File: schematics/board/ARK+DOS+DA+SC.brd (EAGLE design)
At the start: 82 x 92 mm, 210 parts, among them IC2 STM32F103C8T

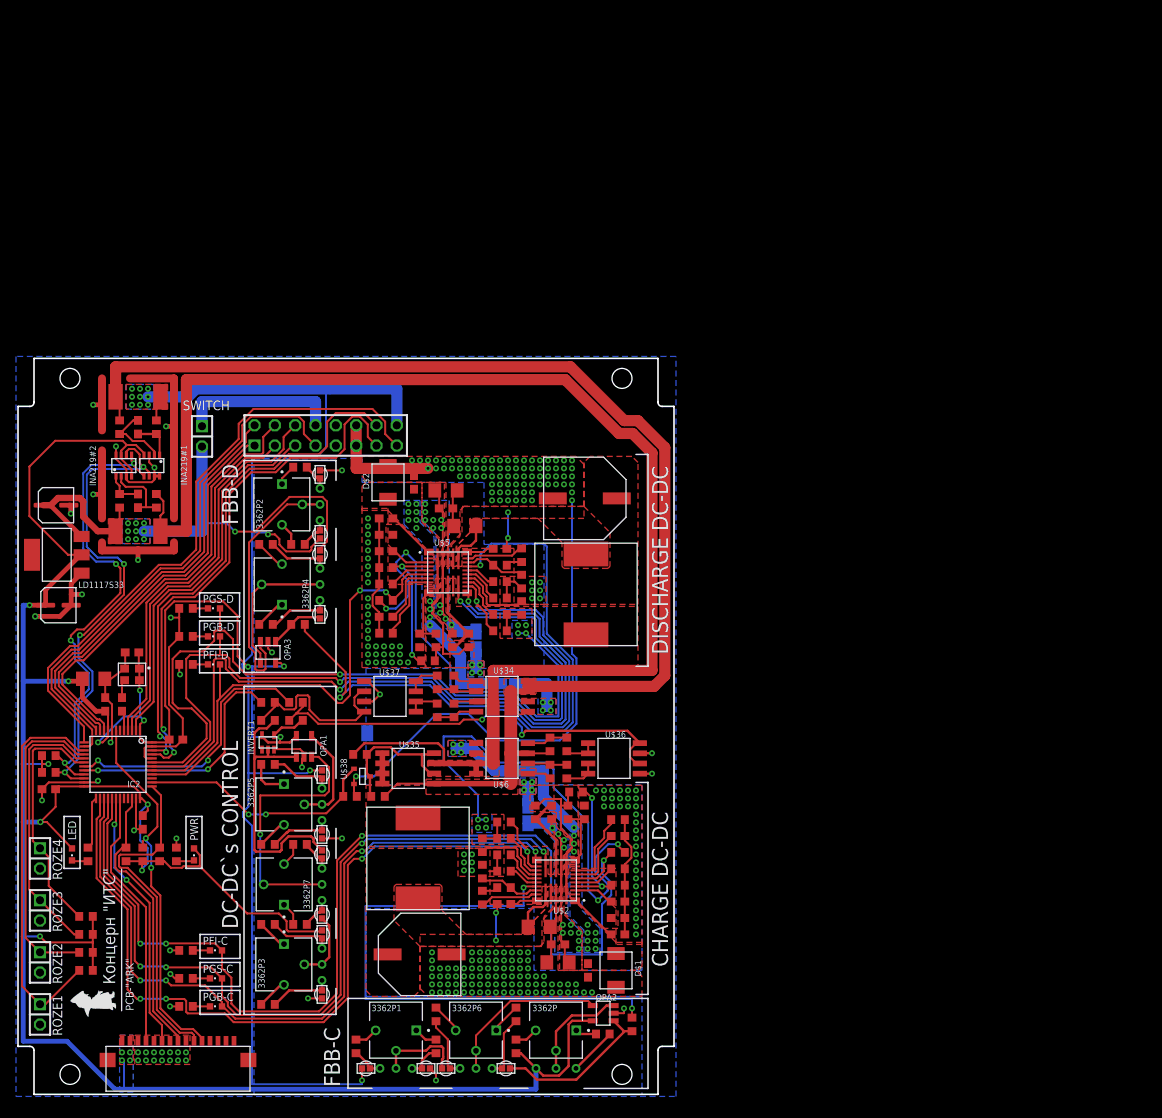
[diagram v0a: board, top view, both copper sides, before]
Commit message: Плата АРК и платы регулярок отправлены в производство
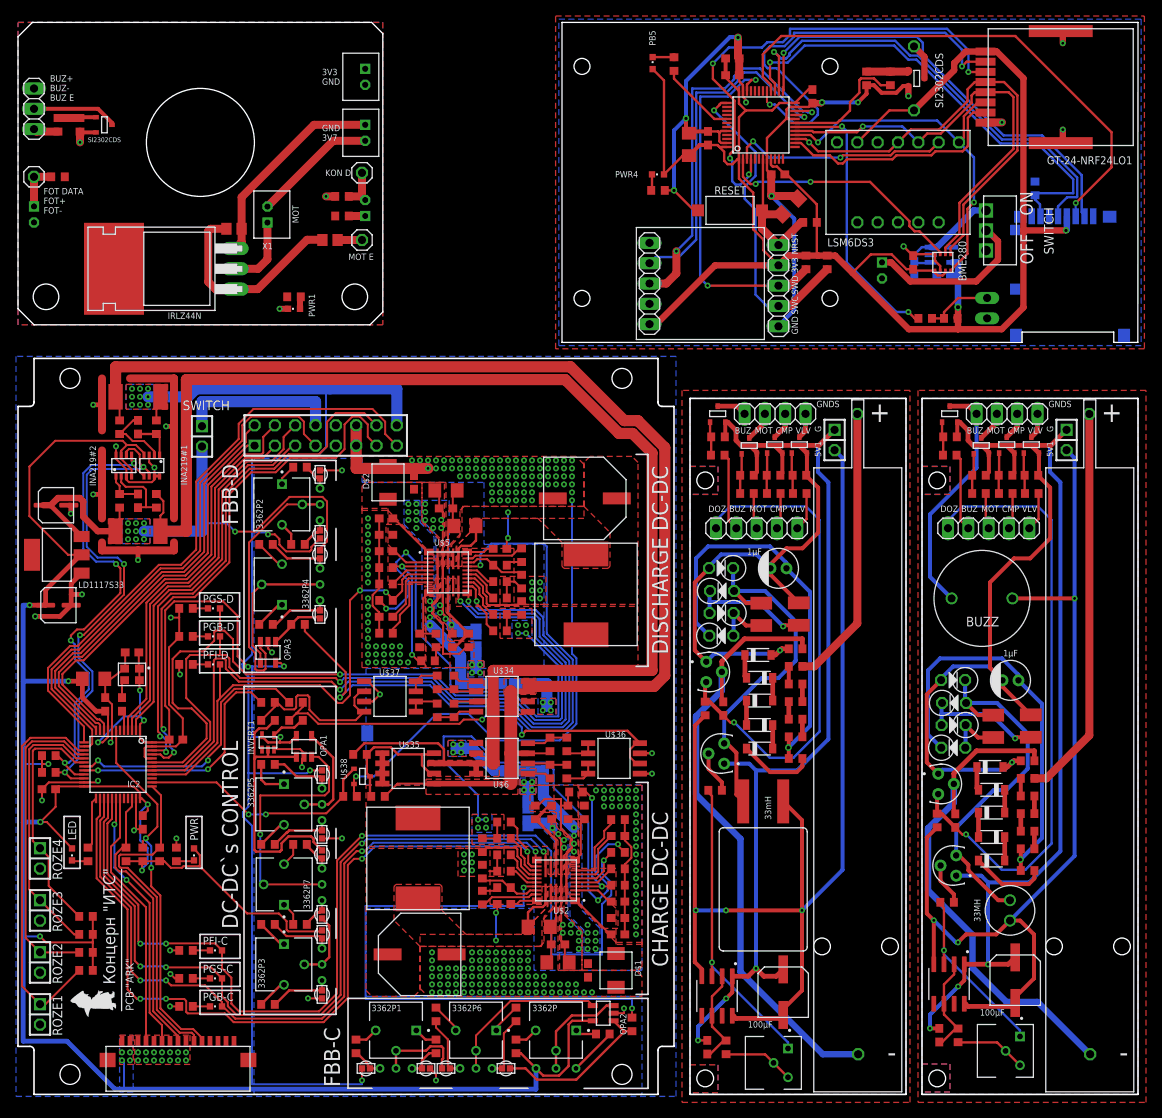
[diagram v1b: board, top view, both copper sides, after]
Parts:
- added BME280: BME280CHIP, CanCubeSat:BME280CHIP
- added BUZZ: BUZZER, CanCubeSat:BUZZER
- added BUZZER: BUZZERS8R6, CanCubeSat:BUZZER-S8R12
- added C12, C19: 100μF, CanCubeSat:ECAP100-CMD
- added C13, C20: 1μF, CanCubeSat:ECAP1MK
- added C14, C15, C21, C22: 22nF, rcl:C1210
- added C17, C23: 100pF, rcl:C0603
- added C18, C25, C27, C28, C29, C3, C30, C31: 100nF, rcl:C0603
- added C24, C32: 1μF, rcl:C0603
- added C26, C33: 10µ, rcl:C1206
- added COM, JP2, JP4: (no value), pinhead:1X01
- added D1, D10, D2, D3, D4, D5, D6, D7, D8, D9: MBR, CanCubeSat:SOD123
- added DEVICE, DEVICE1: DEVICE, pinhead:1X05
- added DOSE, DOSE1: DOSE, CanCubeSat:DOSIM_SBM20-1
- added GND-DEVICE: GND-DEV, pinhead:1X04
- added GND-DEVICE1: GND-DEVICE, pinhead:1X04
- added GOOUUUATGM336H: GOOUUUATGM336H, CanCubeSat:GOOUUUATGM336H
- added GT-24-NRF24LO1: GT-24-NRF24LO1, CanCubeSat:GT-24-NRF24LO1
- added IC1: STM32F103, CanCubeSat:LQFP48
- added IRLZ44N: IRLZ44N, CanCubeSat:TO220H
- added JP3: (no value), pinhead:1X03
- added JP5: (no value), pinhead:1X05
- added LP5907MFX-3.3: (no value), CanCubeSat:5PINSOT23
- added LSM6DS3: LSM6DS3-GY, CanCubeSat:LSM6DS3-GY
- added PB5, PWR1, PWR4: (no value), led:CHIPLED_0603
- added PWR2, PWR3: PWR, CanCubeSat:1X02
- added R100, R36, R55, R58, R59, R61, R83, R86, R87, R89: 10k, rcl:R0603
- added R103, R107, R110: 5k1, resistor:R0603
- added R104, R30, R37, R56, R57, R60, R62, R84, R85, R88, R90, R99: 100R, rcl:R0603
- added R105, R106, R32: 10K, rcl:R0603
- added R108, R109, R50: 1k, resistor:R0603
- added R33: 5k1, rcl:R0603
- added R51: 100R, rcl:R0805
- added R52: 10K, rcl:R0805
- added R53, R78: 1k, rcl:R0603
- added R54, R80: 3k3, rcl:R0603
- added R63, R91: 4k7, rcl:R0603
- added R65, R92: 22k, rcl:R0603
- added R66, R67, R68, R69, R70, R93, R94, R95, R96, R97: 1M, rcl:R0603
- added R72, R98: 100k, rcl:R0603
- added RESET: SMDSWITCH, GC:SMDSWITCH
- added RT1, RT3: 2N6517, CanCubeSat:TO92/TO226
- added RT2, RT4: BC546, CanCubeSat:TO92/TO226
- added SD: SD-SPI, CanCubeSat:SD
- added SI2302-1, SI2302-2, SI2302-3, SI2302-4, SI2302-5, SI2302-6, SI2302-7, SI2302-8, SI2302CDS, SI2302CDS1: SI2302CDS, CanCubeSat:SOT23-3
- added SWITCH1: MSS12D01, CanCubeSat:MSS12D01
- added TOMA: (no value), pinhead:1X02/90
- added U$56, U$57, U$58, U$60, U$61, U$62, U$63, U$8: BA159, CanCubeSat:BA159
- added U$59: 33mH, CanCubeSat:RCH114NP_-
- added U$64: 33MH, CanCubeSat:33MH
- added U1, U2: LMC555, LMC555CMX_NOPB:SOIC127P599X175-8N
- added VR1, VR2: 3362H, CanCubeSat:TRIM_3362H-1-502LF
- added X1, X2, X3, X4, X5: JST-2-KL, CanCubeSat:B2B-PH-K-S
- added X6: JST-2-K-S, CanCubeSat:B2B-PH-K-S
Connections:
- new net 3V1: JP3.3, R33.2, R37.1, R50.1, X4.1
- new net 3V2: BME280.6, BME280.8, BUZZER.P$2, C24.2, C25.1, C26.1, C27.2, C28.1, C29.1, C30.1, C31.1, GOOUUUATGM336H.5, GT-24-NRF24LO1.1, IC1.1, IC1.24, IC1.36, IC1.48, IC1.9, JP5.4, LP5907MFX-3.3.5, LSM6DS3.P$6, PB5.A, PWR4.A, R103.1, R106.2, R107.1, R110.1, SD.VDD
- new net 3V7: C32.2, LP5907MFX-3.3.1, LP5907MFX-3.3.3, SWITCH1.TO2
- new net 3V7-OUT: SWITCH1.FROM, X6.1
- new net 5V1: C12.P$2, PWR2.2, R54.1, U$59.P$1, U1.4, U1.8
- new net 5V3: BUZZ.P$2, C19.P$2, PWR3.2, R80.1, U$64.P$1, U2.4, U2.8
- new net BUZZER: DEVICE.2, R62.2
- new net BUZZER1: DEVICE1.2, R90.2
- new net CE-NRF24LO1: GT-24-NRF24LO1.2, IC1.29
- new net DOZIMETR: C17.2, DEVICE.1, R54.2, RT2.3
- new net DOZIMETR1: C23.2, DEVICE1.1, R80.2, RT4.3
- new net DVIG: DEVICE.4, R57.2
- new net DVIG1: DEVICE1.4, R85.2
- new net GND-BUZZER: GND-DEVICE.1, SI2302-1.3
- new net GND-BUZZER1: BUZZ.P$1, GND-DEVICE1.1, SI2302-5.3
- new net GND-DVIG: GND-DEVICE.3, SI2302-3.3
- new net GND-DVIG1: GND-DEVICE1.3, SI2302-7.3
- new net GND-MOTOR: GND-DEVICE.2, SI2302-2.3
- new net GND-MOTOR1: GND-DEVICE1.2, SI2302-8.3
- new net GND-VALVE: GND-DEVICE.4, SI2302-4.3
- new net GND-VALVE1: GND-DEVICE1.4, SI2302-6.3
- new net GND1: PWR1.C, R32.2, R36.2, SI2302CDS.2, X2.2, X4.2
- new net GND2: C12.P$1, C13.P$2, C15.2, C3.1, D5.A, PWR2.1, R55.1, R58.1, R59.1, R61.1, R72.1, RT1.1, RT2.1, SI2302-1.2, SI2302-2.2, SI2302-3.2, SI2302-4.2, U$8.P$1, U1.1
- new net GND4: C18.1, C19.P$1, C20.P$2, C22.2, D10.A, PWR3.1, R83.1, R86.1, R87.1, R89.1, R98.1, RT3.1, RT4.1, SI2302-5.2, SI2302-6.2, SI2302-7.2, SI2302-8.2, U$60.P$1, U2.1
- new net GND6: BME280.1, BME280.7, C24.1, C25.2, C26.2, C27.1, C28.2, C29.2, C30.2, C31.2, C32.1, C33.2, GOOUUUATGM336H.4, GT-24-NRF24LO1.8, GT-24-NRF24LO1.P$10, GT-24-NRF24LO1.P$9, IC1.20, IC1.23, IC1.35, IC1.44, IC1.47, IC1.8, JP5.1, LP5907MFX-3.3.2, LSM6DS3.P$5, LSM6DS3.P$8, LSM6DS3.P$9, R100.1, R105.2, R109.1, RESET.2, SD.VSS, SI2302CDS1.2, TOMA.2, X6.2
- new net IRQ-NRF24LO1: GT-24-NRF24LO1.7, IC1.14
- new net MOTOR: DEVICE.3, R60.2
- new net MOTOR1: DEVICE1.3, R88.2
- new net N$103: PWR1.A, R50.2
- new net N$107: COM.1, R33.1, X2.1
- new net N$110: IRLZ44N.3, R52.1, X5.1
- new net N$111: X1.2, X5.2
- new net N$112: C3.2, R53.2, U1.2, U1.6
- new net N$113: R53.1, VR1.2, VR1.3
- new net N$114: R63.1, U1.3, VR1.1
- new net N$115: R63.2, RT1.2
- new net N$116: C14.1, RT1.3, U$56.P$1, U$59.P$2, U$8.P$2
- new net N$117: C15.1, U$56.P$2, U$57.P$1
- new net N$118: C14.2, U$57.P$2, U$58.P$1
- new net N$119: C13.P$1, R65.1, R66.1, U$58.P$2
- new net N$120: D4.A, D5.C
- new net N$121: D3.A, D4.C
- new net N$122: D2.A, D3.C
- new net N$123: D1.A, D2.C
- new net N$124: D1.C, R65.2
- new net N$125: R66.2, R67.2
- new net N$126: R67.1, R68.1
- new net N$127: R68.2, R69.2
- new net N$128: R69.1, R70.1
- new net N$129: DOSE.P$1, R70.2
- new net N$130: R61.2, R62.1, SI2302-1.1
- new net N$131: R59.2, R60.1, SI2302-2.1
- new net N$132: R57.1, R58.2, SI2302-3.1
- new net N$133: R55.2, R56.1, SI2302-4.1
- new net N$134: C17.1, DOSE.P$2, R72.2, RT2.2
- new net N$135: C18.2, R78.2, U2.2, U2.6
- new net N$136: R78.1, VR2.2, VR2.3
- new net N$137: R91.1, U2.3, VR2.1
- new net N$138: R91.2, RT3.2
- new net N$139: C21.1, RT3.3, U$60.P$2, U$61.P$1, U$64.P$2
- new net N$140: C22.1, U$61.P$2, U$62.P$1
- new net N$141: C21.2, U$62.P$2, U$63.P$1
- new net N$142: C20.P$1, R92.1, R93.1, U$63.P$2
- new net N$143: D10.C, D9.A
- new net N$144: D8.A, D9.C
- new net N$145: D7.A, D8.C
- new net N$146: D6.A, D7.C
- new net N$148: D6.C, R92.2
- new net N$149: R93.2, R94.2
- new net N$152: R94.1, R95.1
- new net N$153: R95.2, R96.2
- new net N$154: R96.1, R97.1
- new net N$155: DOSE1.P$1, R97.2
- new net N$156: R89.2, R90.1, SI2302-5.1
- new net N$157: R87.2, R88.1, SI2302-8.1
- new net N$158: R85.1, R86.2, SI2302-7.1
- new net N$160: R83.2, R84.1, SI2302-6.1
- new net N$161: C23.1, DOSE1.P$2, R98.2, RT4.2
- new net N$162: BUZZER.P$1, SI2302CDS1.3
- new net N$163: PWR4.C, R109.2
- new net N$164: IC1.41, R108.1
- new net N$165: PB5.C, R108.2
- new net N$166: R104.1, R106.1, TOMA.1
- new net N$167: IC1.18, R104.2
- new net N$168: R100.2, R99.2, SI2302CDS1.1
- new net N$45: IRLZ44N.2, X1.1
- new net N$82: IRLZ44N.1, R51.2, R52.2
- new net N$84: JP2.1, R51.1
- new net N$85: R30.2, R32.1, SI2302CDS.1
- new net N$87: JP3.2, SI2302CDS.3
- new net N$89: JP3.1, R30.1
- new net N$91: JP4.1, R36.1, X3.2
- new net N$92: R37.2, X3.1
- new net NRST1: C33.1, IC1.7, JP5.5, R110.2, RESET.1
- new net PB1-BUZZER: IC1.19, R99.1
- new net SPI1_CS_BME280: BME280.2, IC1.2
- new net SPI1_CS_LSM6DS3: IC1.3, LSM6DS3.P$2
- new net SPI1_CS_NRF24LO1: GT-24-NRF24LO1.3, IC1.4
- new net SPI1_MISO: BME280.5, GT-24-NRF24LO1.6, IC1.16, LSM6DS3.P$1
- new net SPI1_MOSI: BME280.3, GT-24-NRF24LO1.5, IC1.17, LSM6DS3.P$3
- new net SPI1_SCK: BME280.4, GT-24-NRF24LO1.4, IC1.15, LSM6DS3.P$4
- new net SPI2_CS_SD: IC1.25, SD.DAT3
- new net SPI2_MISO: IC1.27, R105.1, SD.DAT0
- new net SPI2_MOSI: IC1.28, SD.CMD
- new net SPI2_SCK: IC1.26, SD.CLK
- new net SWC1: IC1.37, JP5.2, R103.2
- new net SWD1: IC1.34, JP5.3, R107.2
- new net USART3_RX: GOOUUUATGM336H.3, IC1.22
- new net USART3_TX: GOOUUUATGM336H.2, IC1.21
- new net VALVE: DEVICE.5, R56.2
- new net VALVE1: DEVICE1.5, R84.2
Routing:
- net 3V2: track 0.00 -> 224.4 mm, vias 0 -> 2
- net GND4: track 0.00 -> 199.5 mm, vias 0 -> 4
- net GND2: track 0.00 -> 185.5 mm, vias 0 -> 4
- net 5V1: track 0.00 -> 142.3 mm, vias 0 -> 3
- net 5V3: track 0.00 -> 120.1 mm, vias 0 -> 3
- net GND6: track 0.00 -> 112.7 mm, vias 0 -> 12
- net N$134: track 0.00 -> 77.7 mm
- net DOZIMETR1: track 0.00 -> 76.9 mm, vias 0 -> 1
- net SPI2_MOSI: track 0.00 -> 66.9 mm, vias 0 -> 1
- net N$161: track 0.00 -> 63.5 mm
- net DOZIMETR: track 0.00 -> 62.9 mm, vias 0 -> 1
- net SPI1_CS_NRF24LO1: track 0.00 -> 61.3 mm, vias 0 -> 4
- net SPI2_MISO: track 0.00 -> 59.1 mm, vias 0 -> 1
- net SPI2_SCK: track 0.00 -> 58.1 mm, vias 0 -> 1
- net SPI1_SCK: track 0.00 -> 57.0 mm, vias 0 -> 1
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- added copper zone on layer 1, net 3V1
- added copper zone on layer 1, net 5V1
- added copper zone on layer 1, net 5V2
- added copper zone on layer 1, net 5V3
- added copper zone on layer 1, net 5V4
- added copper zone on layer 16, net GND1
- added copper zone on layer 1, net GND2
- added copper zone on layer 16, net GND2
- added copper zone on layer 16, net GND3
- added copper zone on layer 1, net GND4
- added copper zone on layer 16, net GND4
- added copper zone on layer 16, net GND5
- added copper zone on layer 1, net GND6
- added copper zone on layer 16, net GND6
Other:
- board size 82 x 92 mm -> 140 x 134 mm
- board text added: "+"
- board text added: "-"
- board text added: "3V3 GND"
- board text added: "5V1"
- board text added: "BUZ"
- board text added: "BUZ+ BUZ- BUZ E"
- board text added: "CMP"
- board text added: "DOZ"
- board text added: "FOT DATA FOT+ FOT-"
- board text added: "G"
- board text added: "GND 3V7"
- board text added: "GNDS"
- board text added: "KON D"
- board text added: "KON NO KON COM"
- board text added: "MOT"
- board text added: "MOT E"
- board text added: "OFF"
- board text added: "ON"
- board text added: "SI2302CDS"
- board text added: "SWITCH"
- board text added: "VLV"
